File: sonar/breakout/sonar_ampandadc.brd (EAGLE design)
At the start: 25.4 x 40.8 mm, 19 parts

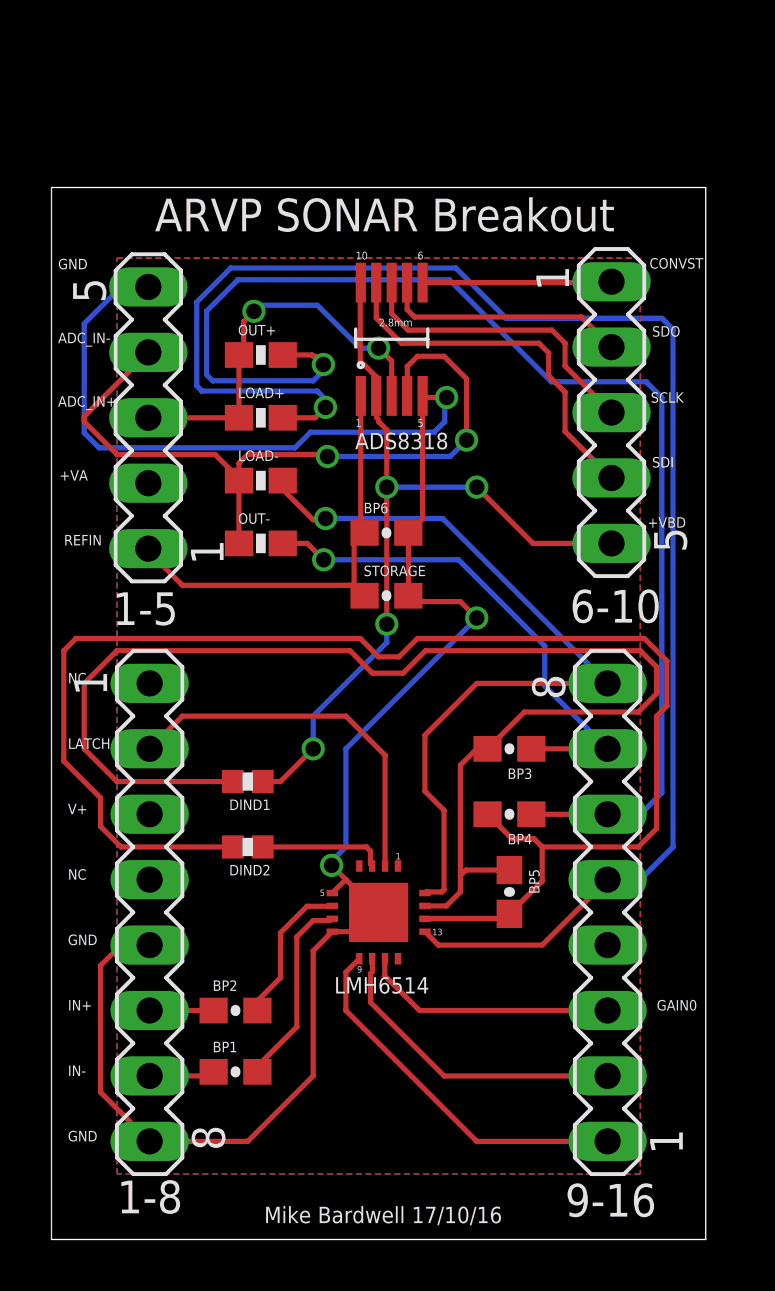
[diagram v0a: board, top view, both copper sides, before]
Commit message: Made requested changes. When ordering be sure to tell them that I added a VSCORE layer in the middle of the board
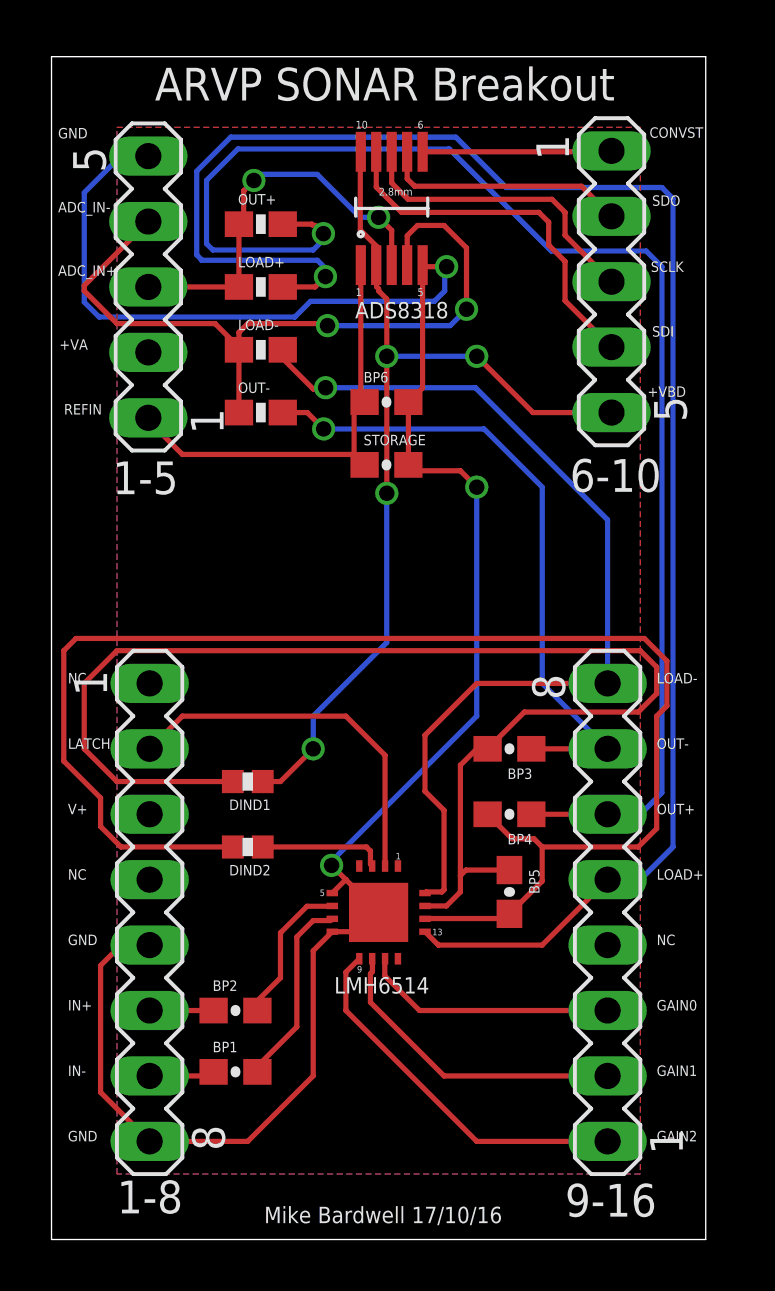
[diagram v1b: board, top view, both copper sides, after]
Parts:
- moved BP6 5.08 mm to (13.0, 32.5)
- moved OUT- 5.08 mm to (8.13, 32.1)
- moved 1-5 5.08 mm to (3.76, 37.0)
- moved 6-10 5.08 mm to (21.7, 37.2)
- moved LOAD+ 5.08 mm to (8.13, 37.0)
- moved LOAD- 5.08 mm to (8.13, 34.5)
- moved OUT+ 5.08 mm to (8.13, 39.4)
- moved STORAGE 5.08 mm to (13.0, 30.1)
- moved U$2 5.08 mm to (13.2, 40.0)
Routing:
- net LOAD-: track 31.1 -> 37.0 mm
- net OUT--: track 19.8 -> 25.4 mm
- net V+: track 36.7 -> 41.8 mm
- net OUT++: track 50.1 -> 55.1 mm
- net LOAD+: track 62.2 -> 67.2 mm
- net GND: track 75.4 -> 80.5 mm
- net OUT-: track 50.9 -> 50.2 mm
- net OUT+: track 58.0 -> 57.4 mm
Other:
- board size 25.4 x 40.8 mm -> 25.4 x 45.9 mm
